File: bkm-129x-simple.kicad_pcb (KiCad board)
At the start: 2 copper layers, 105 x 89.3 mm, 55 parts, among them J1 YG1, J2 PBB1, J3 PRR1, J4 SYNC1, J5 Conn_02x32_Row_Letter_Last, Q1 DTC144EKA, U1 ADG1611, U2 THS7374, U3 arduino-nano-v3, U4 74LVC125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

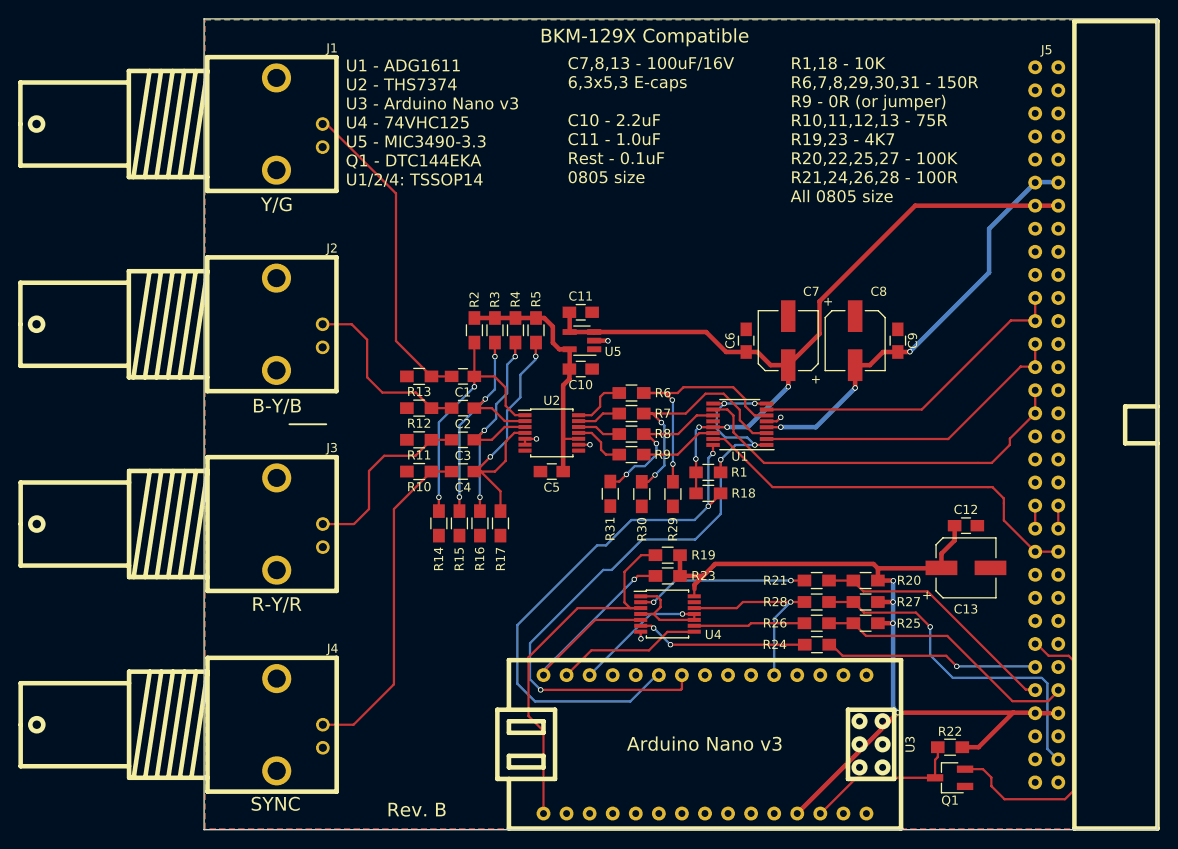
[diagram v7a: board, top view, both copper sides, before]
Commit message: Rearranged some components, bumped to rev. C
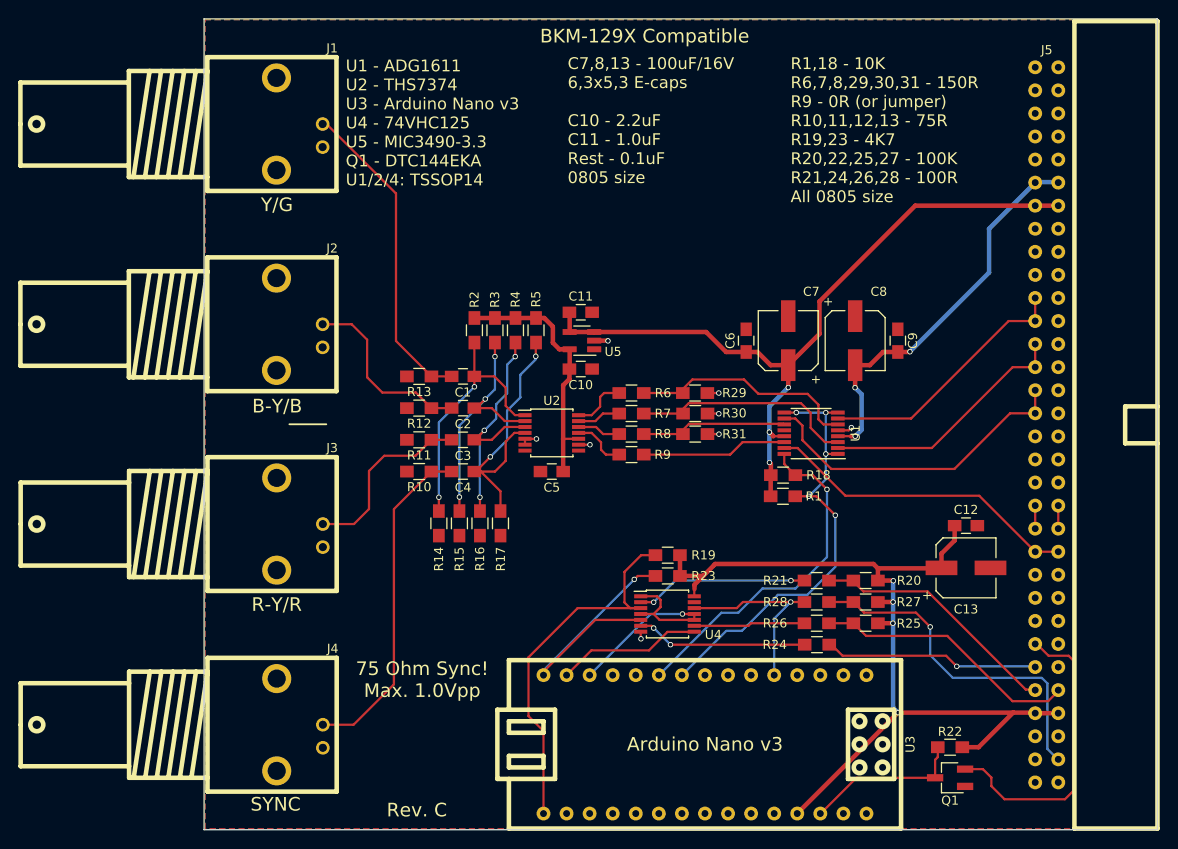
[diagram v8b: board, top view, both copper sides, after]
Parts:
- moved R31 11.4 mm to (175.1, 107.6), turned to 0 degrees
- moved R29 11.4 mm to (175.1, 103.0), turned to 0 degrees
- moved R30 10.6 mm to (175.1, 105.3), turned to 0 degrees
- moved R1 8.63 mm to (184.8, 114.4)
- moved R18 8.48 mm to (184.8, 112.1)
- moved U1 7.91 mm to (187.9, 107.5)
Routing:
- net ~BX_OE: track 76.7 -> 50.0 mm
- net ~EXT_SYNC_OE: track 59.4 -> 38.6 mm, vias 2 -> 1
- net /EXT_SYNC: track 44.6 -> 34.9 mm
- net /P-R/R: track 44.2 -> 35.9 mm
- net Net-(R9-Pad1): track 8.60 -> 16.0 mm
- net /P-B/B: track 35.4 -> 28.0 mm
- net /Y/G: track 36.2 -> 28.8 mm
- net VDD: track 88.4 -> 84.1 mm, vias 4 -> 3
- net VSS: track 47.4 -> 43.7 mm
- net GND: track 7.23 -> 10.9 mm, vias 5 -> 8
- net Net-(R29-Pad1): track 28.0 -> 25.2 mm, vias 2 -> 0
- net Net-(R30-Pad1): track 27.4 -> 24.9 mm, vias 2 -> 0
- net Net-(R31-Pad1): track 17.8 -> 16.6 mm, vias 2 -> 0
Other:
- board text added: "75 Ohm Sync! Max. 1.0Vpp"
- board text added: "Rev. C"
- board text removed: "Rev. B"
